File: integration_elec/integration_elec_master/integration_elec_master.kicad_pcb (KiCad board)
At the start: 4 copper layers, 135.5 x 140 mm, 62 parts, among them J2 USB_C_Receptacle_USB2.0_16P, Q1 Q_NMOS_GSD, SW1 SW_Push, U2 STM32F446RETx, U3 USBLC6-2SC6, U4 TPS54335ADDAR, U5 COM-28379, U6 COM-09032

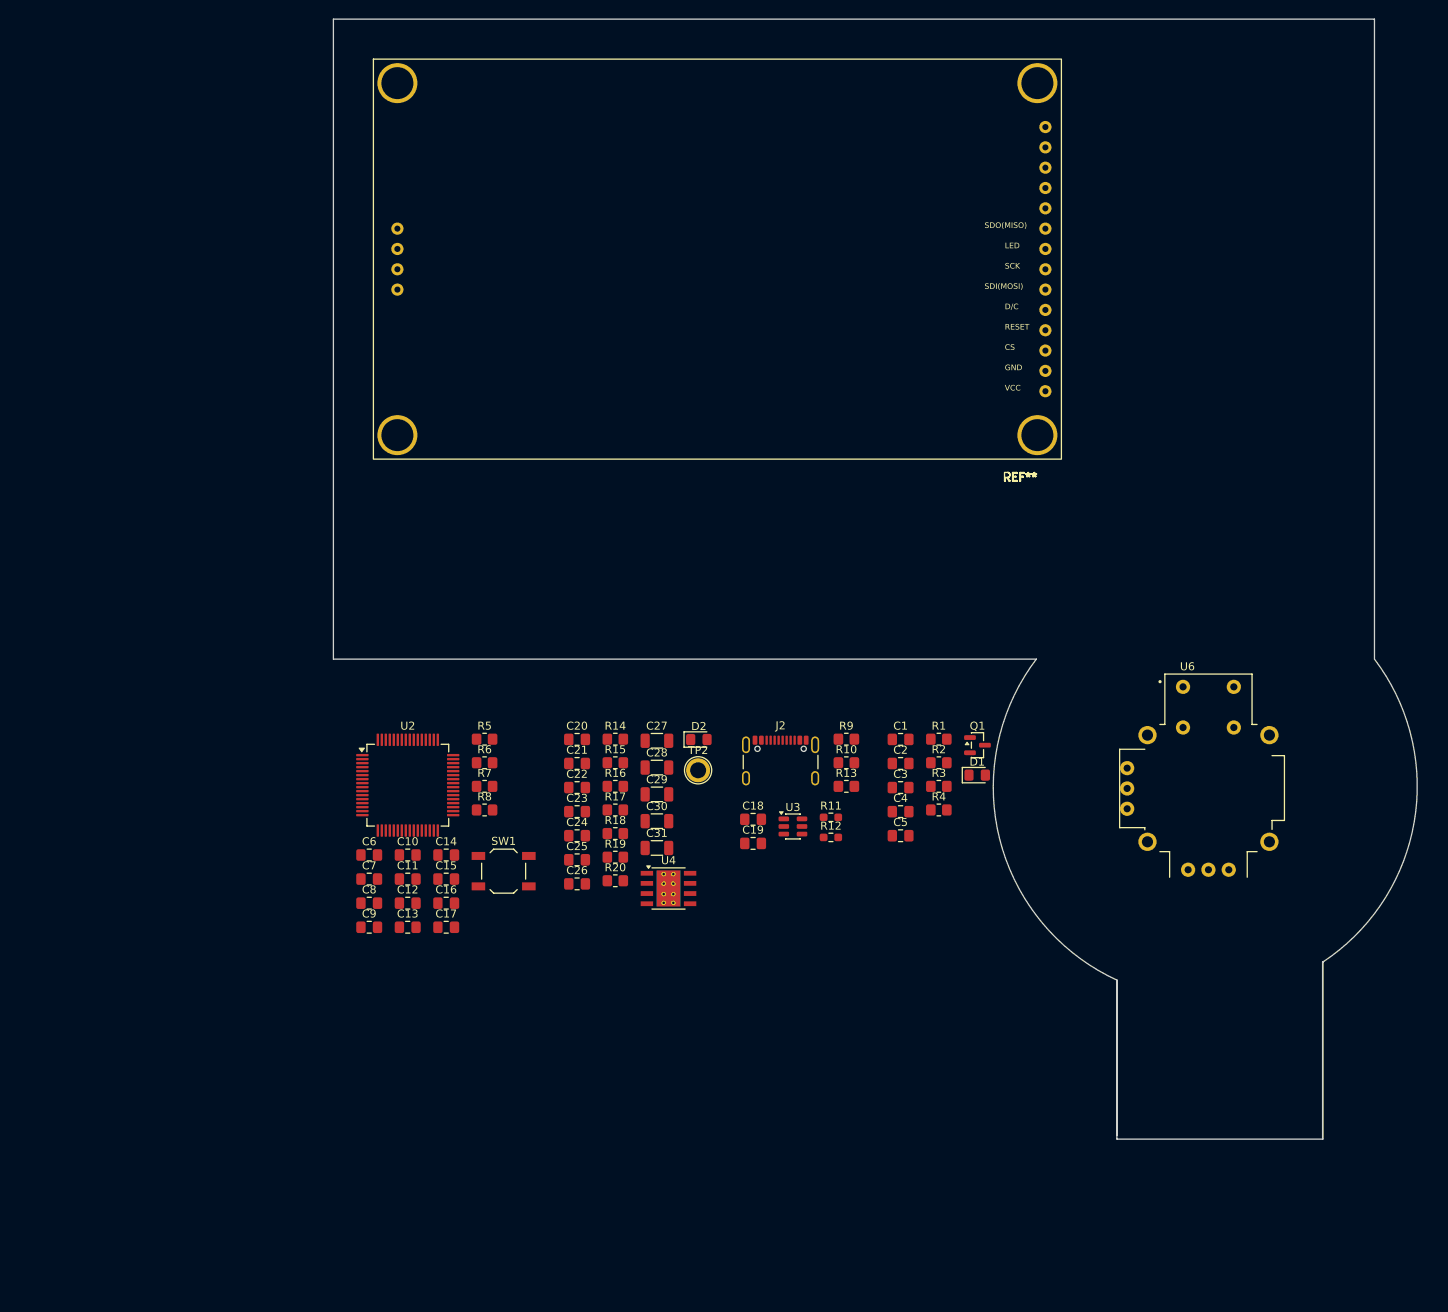
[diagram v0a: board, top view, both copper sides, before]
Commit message: Added plein de footprint
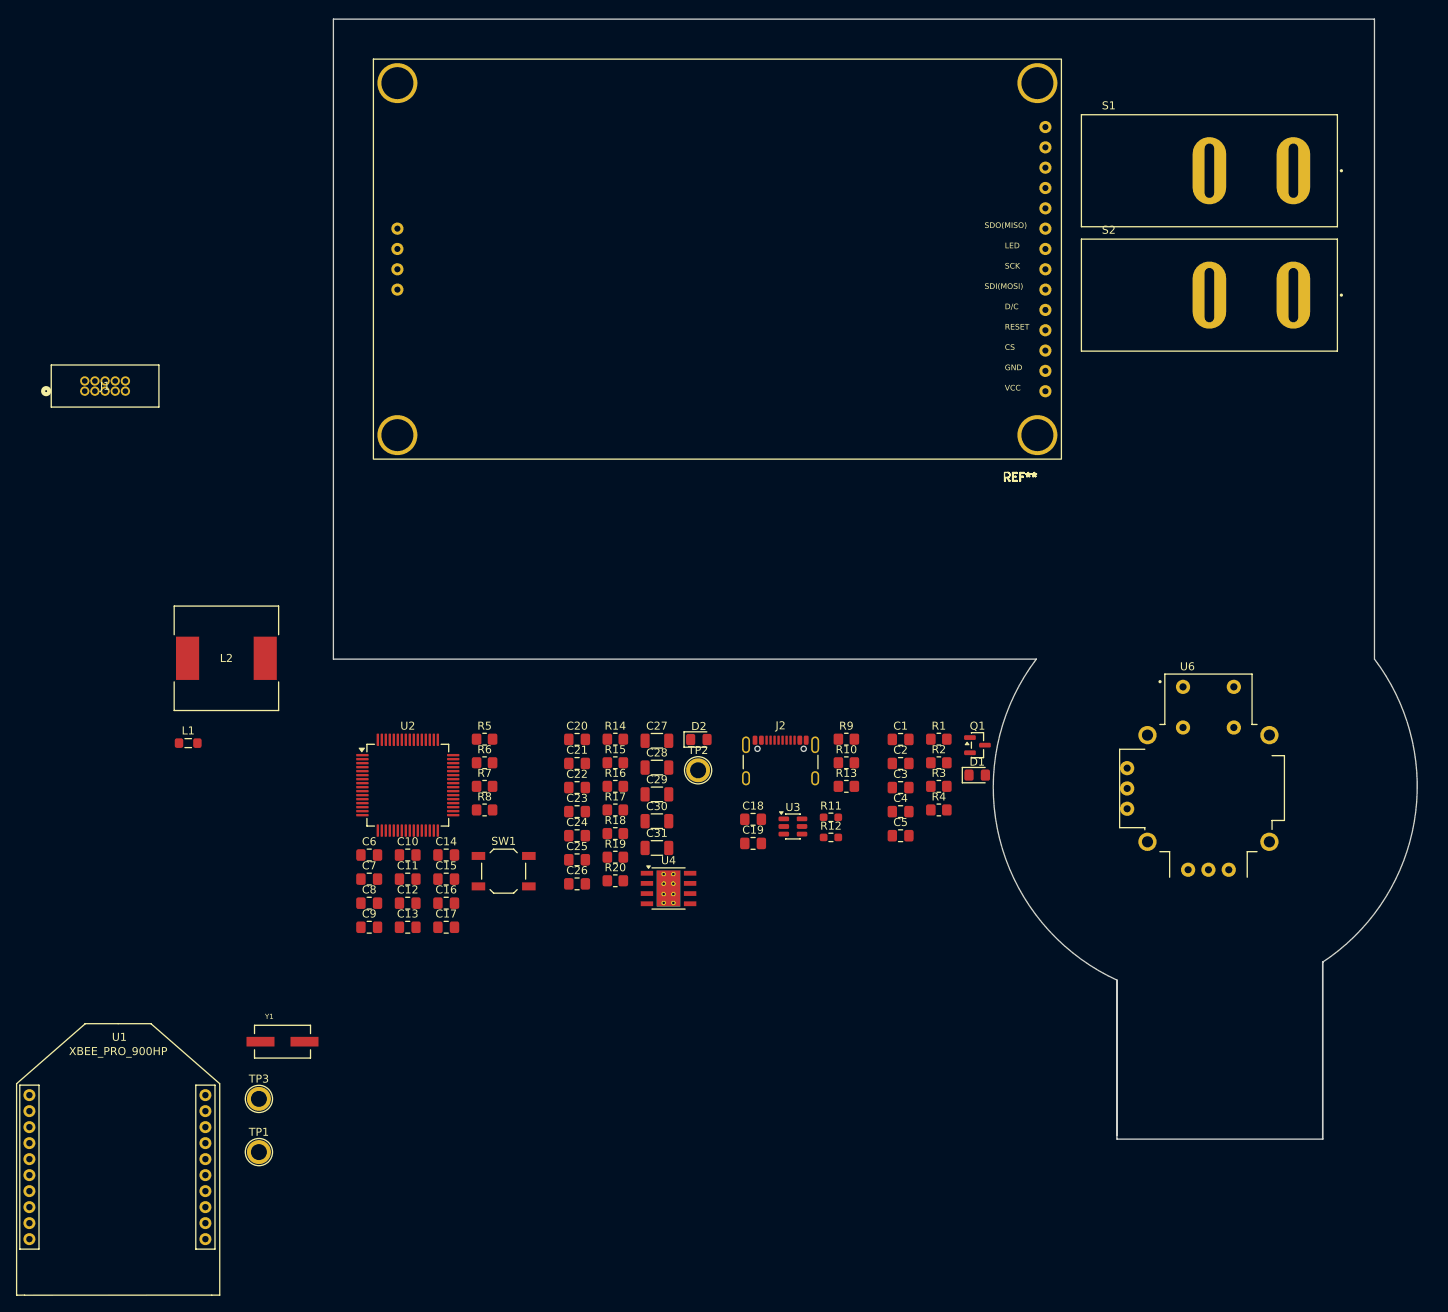
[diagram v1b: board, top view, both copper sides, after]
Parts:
- added J1: CONN_02X05, JOYSTICK:CONN_3220-10-0100-00_CNC, F.Cu at (38.9, 71.5)
- added L1: FerritBead 600 OHM, Inductor_SMD:L_0805_2012Metric_Pad1.05x1.20mm_HandSolder, F.Cu at (51.9, 115.5)
- added L2: 15 uH, JOYSTICK:IND_BOURNS_SRR1280, F.Cu at (56.6, 104.9)
- added S1: RB141C1100, JOYSTICK:SWITCH, F.Cu at (179.5, 44.0)
- added S2: RB141C1100, JOYSTICK:SWITCH, F.Cu at (179.5, 59.5)
- added TP1: 5V_testpoint, TestPoint:TestPoint_Plated_Hole_D2.0mm, F.Cu at (60.7, 166.6)
- added TP3: 3V3_TP, TestPoint:TestPoint_Plated_Hole_D2.0mm, F.Cu at (60.7, 160.0)
- added U1: XBEE_PRO_900HP, JOYSTICK:XBEE_900HP, F.Cu at (32.0, 159.5)
- added Y1: Crystal_16MHz, JOYSTICK:XTAL_ECS-160-20-3X-TR, F.Cu at (63.6, 152.8)
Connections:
- U2 pad 39: unconnected-(U2-PC8-Pad39) -> /MCU/VALVE_1
- U2 pad 40: unconnected-(U2-PC9-Pad40) -> /MCU/VALVE_2

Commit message: Layout started
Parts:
- C18, J2, R10, R11, R12, R9, U1, U3: moved to B.Cu
- moved U1 160.9 mm to (129.1, 31.2), turned to 180 degrees
- moved J1 159.1 mm to (196.0, 96.6), turned to 90 degrees
- moved C12 116.9 mm to (184.5, 84.5), turned to 90 degrees
- moved TP1 107.0 mm to (140.0, 94.8)
- moved C11 105.8 mm to (179.5, 98.5), turned to 180 degrees
- moved C13 103.4 mm to (167.5, 84.5), turned to 90 degrees
- moved L2 102.2 mm to (158.5, 97.2)
- moved U2 101.6 mm to (176.0, 89.5)
- moved C14 101.1 mm to (172.5, 80.5)
- moved C15 95.2 mm to (173.0, 98.5), turned to 180 degrees
- moved U4 62.7 mm to (153.1, 86.4), turned to 90 degrees
- moved C27 59.4 mm to (163.0, 87.5), turned to 90 degrees
- moved R12 39.5 mm to (115.0, 91.8), turned to 180 degrees
- moved R11 35.3 mm to (119.8, 91.8)
- moved U3 31.3 mm to (125.0, 94.8)
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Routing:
- net (no net): vias 0 -> 4
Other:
- board size 135.5 x 140 mm -> 137.3 x 140 mm

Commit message: KAH - Fini schematic attente de review + correction BUS
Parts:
- removed U6: COM-09032, JOYSTICK:XDCR_COM-09032
- added R10: 0, Resistor_SMD:R_0805_2012Metric_Pad1.20x1.40mm_HandSolder, F.Cu at (93.0, 153.8)
- added R5: 0, Resistor_SMD:R_0805_2012Metric_Pad1.20x1.40mm_HandSolder, F.Cu at (93.0, 150.8)
- C11, C12, C13, C14, C15, C27, J1, L2, U2, U4: moved to B.Cu
- C18, J2, U3: moved to F.Cu
- R11: renamed from R9; moved to F.Cu
- R12: renamed from R10; moved to F.Cu
- R13: renamed from R11; moved to F.Cu
- R14: renamed from R12; moved to F.Cu
- moved J1 131.3 mm to (64.8, 91.8)
- moved S2 113.1 mm to (66.5, 58.5), turned to 90 degrees
- moved C12 80.7 mm to (107.9, 59.2)
- moved C11 71.3 mm to (112.9, 73.2), turned to 0 degrees
- moved U2 64.8 mm to (116.4, 64.2), turned to 180 degrees
- moved C14 60.4 mm to (117.6, 55.2), turned to 180 degrees
- moved C15 59.4 mm to (119.3, 73.2), turned to 0 degrees
- moved C13 49.6 mm to (124.9, 59.2)
- moved C27 42.1 mm to (129.4, 62.2)
- moved L2 35.3 mm to (133.9, 71.9), turned to 180 degrees
- moved U4 28.8 mm to (139.3, 61.1)
- moved R11 21.6 mm to (109.3, 87.2), turned to 180 degrees
- moved R12 21.6 mm to (109.3, 91.4), turned to 180 degrees
- moved R15 15.8 mm to (112.3, 96.2)
- moved S1 15.7 mm to (173.5, 58.5), turned to 90 degrees
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- renumbered R13 to R15, R14 to R16, R15 to R17, R16 to R18, R17 to R19, R18 to R20, R19 to R21, R20 to R22, R5 to R6, R6 to R7, R7 to R8, R8 to R9
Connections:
- net /MCU/USB_VBUS renamed /DEBUG_USB/USB_VBUS
- C3 pad 2: /XBEE/RF.XBEE_nReset -> /MCU/RF.XBEE_nReset
- C7 pad 1: /MCU/DEBUG_RESET -> /DEBUG_USB/DEBUG_RESET
- J1 pad 1: unconnected-(J1-P1-Pad1) -> /DEBUG_USB/DEBUG_NJTRST
- J1 pad 3: unconnected-(J1-P3-Pad3) -> /DEBUG_USB/DEBUG_SWO_TDI
- J1 pad 5: unconnected-(J1-P5-Pad5) -> /DEBUG_USB/DEBUG_SWO_TDO
- Q1 pad 1: /XBEE/RF.XBEE_LED -> /MCU/RF.XBEE_LED
- R2 pad 1: /XBEE/RF.XBEE_RQ -> /MCU/RF.XBEE_RQ
- R3 pad 2: /XBEE/RF.XBEE_LED -> /MCU/RF.XBEE_LED
- R7 pad 2: /MCU/DEBUG_RESET -> /DEBUG_USB/DEBUG_RESET
- S1 pad 2: /TFT_SCREEN AND JOYSTICK/VALVE_1 -> /MCU/VALVE_1
- S2 pad 2: /TFT_SCREEN AND JOYSTICK/VALVE_2 -> /MCU/VALVE_2
- SW1 pad 2: /MCU/DEBUG_RESET -> /DEBUG_USB/DEBUG_RESET
- U1 pad 12: /XBEE/RF.XBEE_UART_CTS -> /MCU/RF.XBEE_UART_CTS
- U1 pad 13: /XBEE/RF.XBEE_STATUS -> /MCU/RF.XBEE_STATUS
- U1 pad 15: /XBEE/RF.XBEE_LED -> /MCU/RF.XBEE_LED
- U1 pad 16: /XBEE/RF.XBEE_UART_RTS -> /MCU/RF.XBEE_UART_RTS
- U1 pad 2: /XBEE/RF.XBEE_UART_OUT -> /MCU/RF.XBEE_UART_OUT
- U1 pad 3: /XBEE/RF.XBEE_UART_IN -> /MCU/RF.XBEE_UART_IN
- U1 pad 5: /XBEE/RF.XBEE_nReset -> /MCU/RF.XBEE_nReset
- U2 pad 14: /MCU/X_VALUE -> unconnected-(U2-PA0-Pad14)
- U2 pad 15: /MCU/Y_VALUE -> unconnected-(U2-PA1-Pad15)
- U2 pad 16: /MCU/RESET -> Net-(U2-PA2)
- U2 pad 25: /MCU/DEBUG_UART_RX -> /DEBUG_USB/DEBUG_UART_RX
- U2 pad 29: /MCU/DEBUG_UART_TX -> /DEBUG_USB/DEBUG_UART_TX
- U2 pad 33: /MCU/USB_ID -> unconnected-(U2-PB12-Pad33)
- U2 pad 35: /MCU/USB_D- -> /DEBUG_USB/USB_D-
- U2 pad 36: /MCU/USB_D+ -> /DEBUG_USB/USB_D+
- U2 pad 38: unconnected-(U2-PC7-Pad38) -> /MCU/VALVE_1
- U2 pad 39: /MCU/VALVE_1 -> /MCU/VALVE_2
- U2 pad 40: /MCU/VALVE_2 -> /MCU/RF.XBEE_STATUS
- U2 pad 46: /MCU/DEBUG_SWDIO_TMS -> /DEBUG_USB/DEBUG_SWDIO
- U2 pad 49: /MCU/DEBUG_SWCLK_TCK -> /DEBUG_USB/DEBUG_SWCLK
- U2 pad 50: /MCU/DEBUG_SWO_TDI -> /DEBUG_USB/DEBUG_SWO_TDI
- U2 pad 51: unconnected-(U2-PC10-Pad51) -> /MCU/RF.XBEE_nReset
- U2 pad 55: /MCU/DEBUG_SWO_TDO -> /DEBUG_USB/DEBUG_SWO_TDO
- U2 pad 56: /MCU/DEBUG_NJTRST -> /DEBUG_USB/DEBUG_NJTRST
- U2 pad 7: /MCU/DEBUG_RESET -> /DEBUG_USB/DEBUG_RESET
- U5 pad 3: /TFT_SCREEN AND JOYSTICK/CS_TFT -> /MCU/CS_TFT
- U5 pad 4: /TFT_SCREEN AND JOYSTICK/RESET -> /MCU/RESET_TFT
- U5 pad 5: /TFT_SCREEN AND JOYSTICK/D/C -> /MCU/D/C
- U5 pad 6: /TFT_SCREEN AND JOYSTICK/MOSI -> /MCU/MOSI
- U5 pad 7: /TFT_SCREEN AND JOYSTICK/SCK -> /MCU/SCK
- U5 pad 9: /TFT_SCREEN AND JOYSTICK/MISO -> /MCU/MISO
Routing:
- net (no net): vias 4 -> 2
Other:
- board size 137.3 x 140 mm -> 128 x 74.8 mm
